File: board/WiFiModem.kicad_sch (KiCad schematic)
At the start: 49 parts, among them J1 DB9_Female, J2 DB25_Female, J3 Barrel_Jack_Switch, J4 PRG, SW1 SW_Push, SW2 SW_Push, U1 ESP-12E, U2 LM7805_TO220, U3 MAX232, U4 LT1117-3.3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

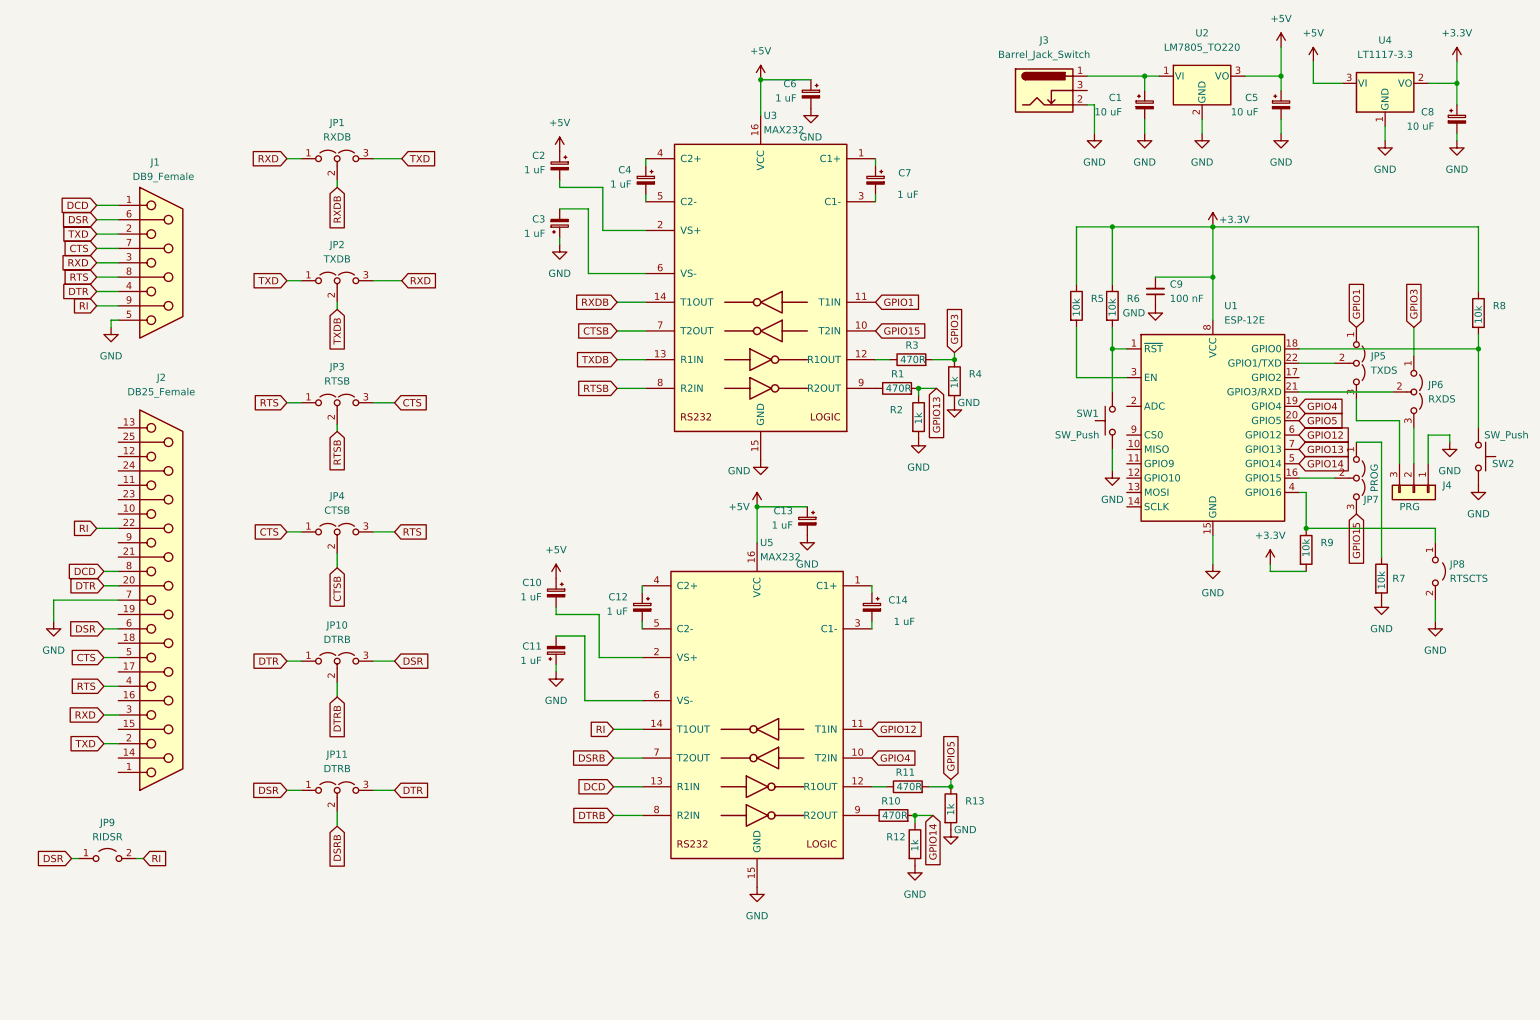
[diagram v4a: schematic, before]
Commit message: Fixed GPIO15 booting issue, changed DCD/DSR/DTR jumper
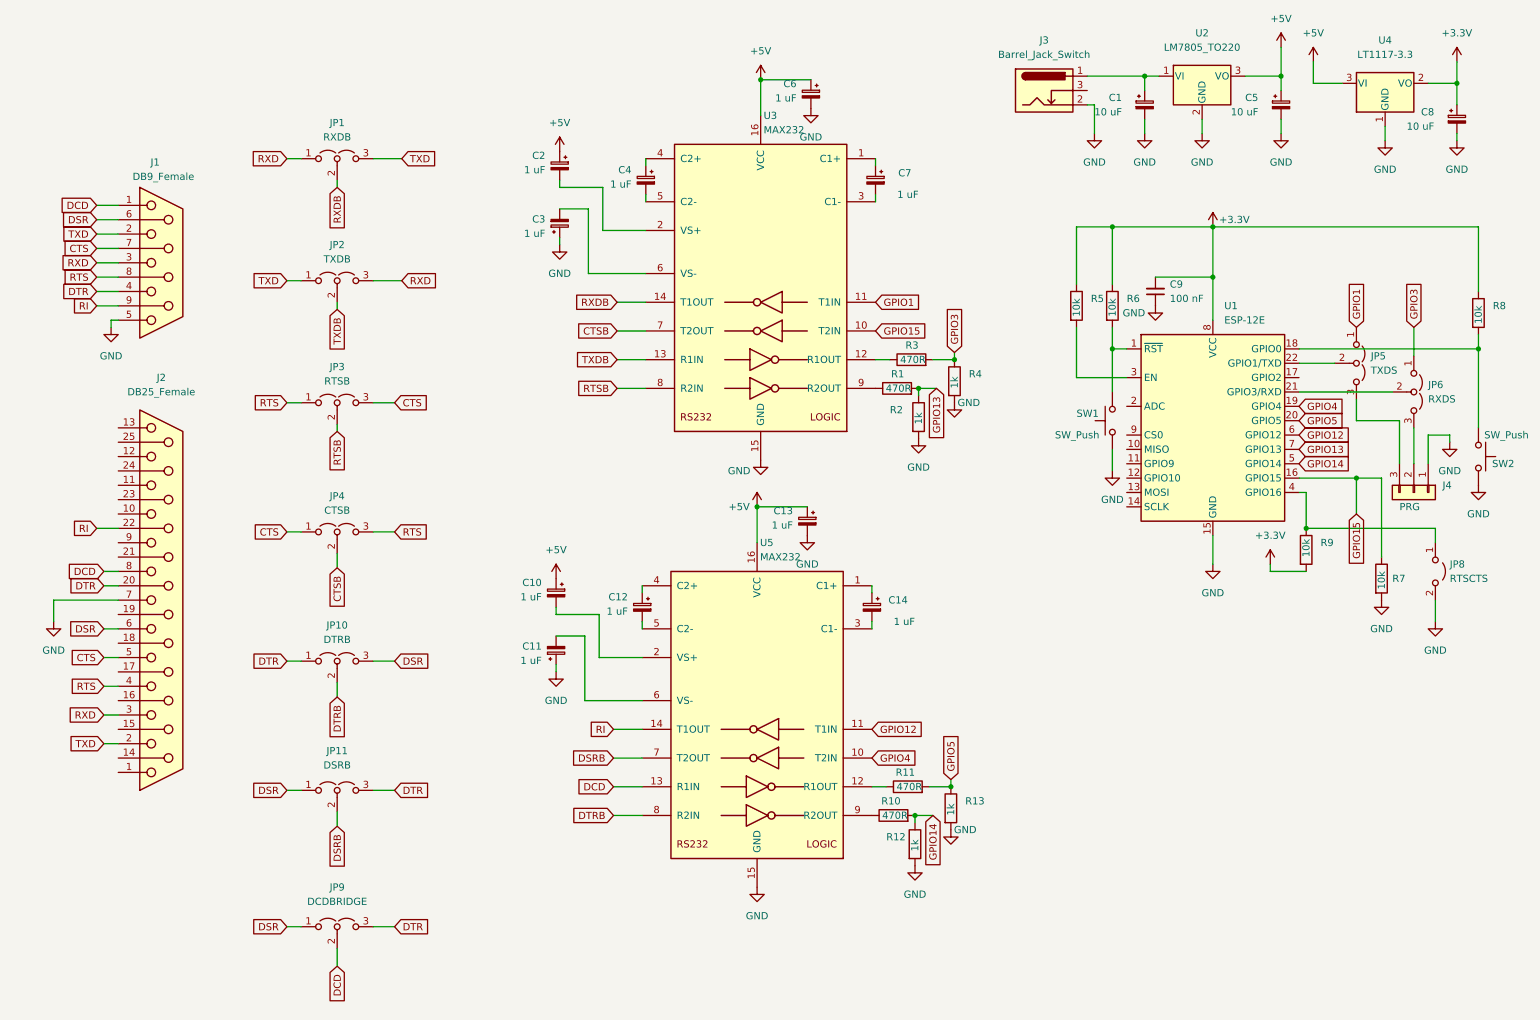
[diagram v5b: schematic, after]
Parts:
- removed JP7: PROG, Connector_PinHeader_2.54mm:PinHeader_1x03_P2.54mm_Vertical, symbol Jumper:Jumper_3_Open
- removed JP9: RIDSR, Connector_PinHeader_2.54mm:PinHeader_1x02_P2.54mm_Vertical, symbol Jumper:Jumper_2_Open
- added JP9: DCDBRIDGE, Connector_PinHeader_2.54mm:PinHeader_1x03_P2.54mm_Vertical, symbol Jumper:Jumper_3_Open
- JP11: value DTRB -> DSRB
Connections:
- net DCD: now also JP9.2 (C)
- net DSR: now also JP9.1 (A)
- net DTR: now also JP9.3 (B)
- net GPIO15: now also R7.1, U1.16 (GPIO15)
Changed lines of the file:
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@@
   (junction (at 175.895 156.21) (diameter 0) (color 0 0 0 0)
   )
+  (junction (at 254 96.52) (diameter 0) (color 0 0 0 0)
+  )
   (wire (pts (xy 80.01 151.765) (xy 83.82 151.765))
     (stroke (width 0) (type default) (color 0 0 0 0))
@@
     (stroke (width 0) (type default) (color 0 0 0 0))
   )
-  (wire (pts (xy 26.67 163.83) (xy 27.94 163.83))
-    (stroke (width 0) (type default) (color 0 0 0 0))
-  )
   (wire (pts (xy 176.53 80.645) (xy 179.705 80.645))
     (stroke (width 0) (type default) (color 0 0 0 0))
@@
     (stroke (width 0) (type default) (color 0 0 0 0))
   )
+  (wire (pts (xy 254 96.52) (xy 254 102.87))
+    (stroke (width 0) (type default) (color 0 0 0 0))
+  )
   (wire (pts (xy 147.955 107.95) (xy 147.955 101.6))
     (stroke (width 0) (type default) (color 0 0 0 0))
@@
     (stroke (width 0) (type default) (color 0 0 0 0))
   )
+  (wire (pts (xy 80.01 175.895) (xy 83.82 175.895))
+    (stroke (width 0) (type default) (color 0 0 0 0))
+  )
   (wire (pts (xy 112.395 129.54) (xy 112.395 130.81))
     (stroke (width 0) (type default) (color 0 0 0 0))
@@
     (stroke (width 0) (type default) (color 0 0 0 0))
   )
+  (wire (pts (xy 64.77 175.895) (xy 67.31 175.895))
+    (stroke (width 0) (type default) (color 0 0 0 0))
+  )
   (wire (pts (xy 245.11 105.41) (xy 267.97 105.41))
     (stroke (width 0) (type default) (color 0 0 0 0))
@@
     (stroke (width 0) (type default) (color 0 0 0 0))
   )
-  (wire (pts (xy 258.445 110.49) (xy 258.445 90.17))
+  (wire (pts (xy 254 96.52) (xy 258.445 96.52))
+    (stroke (width 0) (type default) (color 0 0 0 0))
+  )
+  (wire (pts (xy 258.445 110.49) (xy 258.445 96.52))
     (stroke (width 0) (type default) (color 0 0 0 0))
   )
@@
     (stroke (width 0) (type default) (color 0 0 0 0))
   )
-  (wire (pts (xy 38.1 163.83) (xy 39.37 163.83))
-    (stroke (width 0) (type default) (color 0 0 0 0))
-  )
   (wire (pts (xy 245.11 99.06) (xy 245.11 105.41))
     (stroke (width 0) (type default) (color 0 0 0 0))
@@
     (stroke (width 0) (type default) (color 0 0 0 0))
   )
-  (wire (pts (xy 243.84 96.52) (xy 250.19 96.52))
+  (wire (pts (xy 243.84 96.52) (xy 254 96.52))
     (stroke (width 0) (type default) (color 0 0 0 0))
   )
@@
     (stroke (width 0) (type default) (color 0 0 0 0))
   )
+  (wire (pts (xy 73.66 179.705) (xy 73.66 182.88))
+    (stroke (width 0) (type default) (color 0 0 0 0))
+  )
   (wire (pts (xy 168.91 41.275) (xy 168.91 40.005))
     (stroke (width 0) (type default) (color 0 0 0 0))
@@
   )
   (wire (pts (xy 122.555 156.21) (xy 127.635 156.21))
-    (stroke (width 0) (type default) (color 0 0 0 0))
-  )
-  (wire (pts (xy 254 90.17) (xy 258.445 90.17))
     (stroke (width 0) (type default) (color 0 0 0 0))
   )
@@
     )
   )
-  (global_label "DSR" (shape input) (at 26.67 163.83 180) (fields_autoplaced)
-    (effects (font (size 1.27 1.27)) (justify right))
-    (property "Intersheet References" "${INTERSHEET_REFS}" (id 0) (at 20.5074 163.9094 0)
+  (global_label "DSR" (shape input) (at 64.77 175.895 180) (fields_autoplaced)
+    (effects (font (size 1.27 1.27)) (justify right))
+    (property "Intersheet References" "${INTERSHEET_REFS}" (id 0) (at 58.6074 175.9744 0)
       (effects (font (size 1.27 1.27)) (justify right) hide)
     )
@@
     )
   )
-  (global_label "RI" (shape input) (at 39.37 163.83 0) (fields_autoplaced)
-    (effects (font (size 1.27 1.27)) (justify left))
-    (property "Intersheet References" "${INTERSHEET_REFS}" (id 0) (at 43.6579 163.9094 0)
-      (effects (font (size 1.27 1.27)) (justify left) hide)
+  (global_label "DCD" (shape input) (at 73.66 182.88 270) (fields_autoplaced)
+    (effects (font (size 1.27 1.27)) (justify right))
+    (property "Intersheet References" "${INTERSHEET_REFS}" (id 0) (at 73.5806 189.1031 90)
+      (effects (font (size 1.27 1.27)) (justify right) hide)
     )
   )
@@
     (property "Intersheet References" "${INTERSHEET_REFS}" (id 0) (at 73.5806 73.8052 90)
       (effects (font (size 1.27 1.27)) (justify right) hide)
+    )
+  )
+  (global_label "DTR" (shape input) (at 83.82 175.895 0) (fields_autoplaced)
+    (effects (font (size 1.27 1.27)) (justify left))
+    (property "Intersheet References" "${INTERSHEET_REFS}" (id 0) (at 89.7407 175.8156 0)
+      (effects (font (size 1.27 1.27)) (justify left) hide)
     )
   )
@@
   (symbol (lib_id "Jumper:Jumper_3_Open") (at 73.66 151.765 0) (unit 1)
     (in_bom yes) (on_board yes) (fields_autoplaced)
-    (property "Reference" "JP11" (id 0) (at 73.66 145.415 0))
-    (property "Value" "DTRB" (id 1) (at 73.66 147.955 0))
+    (property "Reference" "JP11" (id 0) (at 73.66 144.78 0))
+    (property "Value" "DSRB" (id 1) (at 73.66 147.32 0))
     (property "Footprint" "Connector_PinHeader_2.54mm:PinHeader_1x03_P2.54mm_Vertical" (id 2) (at 73.66 151.765 0)
       (effects (font (size 1.27 1.27)) hide)
@@
     )
     (pin "1")
-  )
-  (symbol (lib_id "Jumper:Jumper_2_Open") (at 33.02 163.83 0) (unit 1)
-    (in_bom yes) (on_board yes) (fields_autoplaced)
-    (property "Reference" "JP9" (id 0) (at 33.02 157.48 0))
-    (property "Value" "RIDSR" (id 1) (at 33.02 160.02 0))
-    (property "Footprint" "Connector_PinHeader_2.54mm:PinHeader_1x02_P2.54mm_Vertical" (id 2) (at 33.02 163.83 0)
-      (effects (font (size 1.27 1.27)) hide)
-    )
-    (property "Datasheet" "~" (id 3) (at 33.02 163.83 0)
-      (effects (font (size 1.27 1.27)) hide)
-    )
-    (pin "1")
-    (pin "2")
   )
   (symbol (lib_id "power:GND") (at 240.665 35.56 0) (mirror y) (unit 1)
@@
     (pin "1")
   )
+  (symbol (lib_id "Jumper:Jumper_3_Open") (at 73.66 175.895 0) (unit 1)
+    (in_bom yes) (on_board yes) (fields_autoplaced)
+    (property "Reference" "JP9" (id 0) (at 73.66 168.91 0))
+    (property "Value" "DCDBRIDGE" (id 1) (at 73.66 171.45 0))
+    (property "Footprint" "Connector_PinHeader_2.54mm:PinHeader_1x03_P2.54mm_Vertical" (id 2) (at 73.66 175.895 0)
+      (effects (font (size 1.27 1.27)) hide)
+    )
+    (property "Datasheet" "~" (id 3) (at 73.66 175.895 0)
+      (effects (font (size 1.27 1.27)) hide)
+    )
+    (pin "1")
+    (pin "2")
+    (pin "3")
+  )
   (symbol (lib_id "power:+5V") (at 240.665 20.32 0) (mirror y) (unit 1)
     (in_bom yes) (on_board yes) (fields_autoplaced)
@@
     )
     (pin "1")
-  )
-  (symbol (lib_id "Jumper:Jumper_3_Open") (at 254 96.52 270) (unit 1)
-    (in_bom yes) (on_board yes)
-    (property "Reference" "JP7" (id 0) (at 255.27 100.33 90)
-      (effects (font (size 1.27 1.27)) (justify left))
-    )
-    (property "Value" "PROG" (id 1) (at 257.175 93.98 0)
-      (effects (font (size 1.27 1.27)) (justify left))
-    )
-    (property "Footprint" "Connector_PinHeader_2.54mm:PinHeader_1x03_P2.54mm_Vertical" (id 2) (at 254 96.52 0)
-      (effects (font (size 1.27 1.27)) hide)
-    )
-    (property "Datasheet" "~" (id 3) (at 254 96.52 0)
-      (effects (font (size 1.27 1.27)) hide)
-    )
-    (pin "1")
-    (pin "2")
-    (pin "3")
   )
   (symbol (lib_id "power:GND") (at 259.08 36.83 0) (mirror y) (unit 1)
@@
       (reference "JP6") (unit 1) (value "RXDS") (footprint "Connector_PinHeader_2.54mm:PinHeader_1x03_P2.54mm_Vertical")
     )
-    (path "/e384ffec-bb2c-46ec-b097-3f0cea4d11a2"
-      (reference "JP7") (unit 1) (value "PROG") (footprint "Connector_PinHeader_2.54mm:PinHeader_1x03_P2.54mm_Vertical")
-    )
     (path "/2cfe946b-ef42-4712-aba1-8371f5f81b04"
       (reference "JP8") (unit 1) (value "RTSCTS") (footprint "Connector_PinHeader_2.54mm:PinHeader_1x02_P2.54mm_Vertical")
     )
-    (path "/6e6f41cf-eea7-4319-a566-0c19ed9572c2"
-      (reference "JP9") (unit 1) (value "RIDSR") (footprint "Connector_PinHeader_2.54mm:PinHeader_1x02_P2.54mm_Vertical")
+    (path "/dafbc4d4-726b-47c7-b074-8d381c5f7477"
+      (reference "JP9") (unit 1) (value "DCDBRIDGE") (footprint "Connector_PinHeader_2.54mm:PinHeader_1x03_P2.54mm_Vertical")
     )
     (path "/d066ecb3-5158-4d54-9143-8be97669845b"
@@
     )
     (path "/5247d984-7f9f-417f-8e7e-3a014e2c2aca"
-      (reference "JP11") (unit 1) (value "DTRB") (footprint "Connector_PinHeader_2.54mm:PinHeader_1x03_P2.54mm_Vertical")
+      (reference "JP11") (unit 1) (value "DSRB") (footprint "Connector_PinHeader_2.54mm:PinHeader_1x03_P2.54mm_Vertical")
     )
     (path "/ed4f2a97-7862-4c00-9260-110c4aa8ea06"

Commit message: Fixed DCD and DB25 pinouts
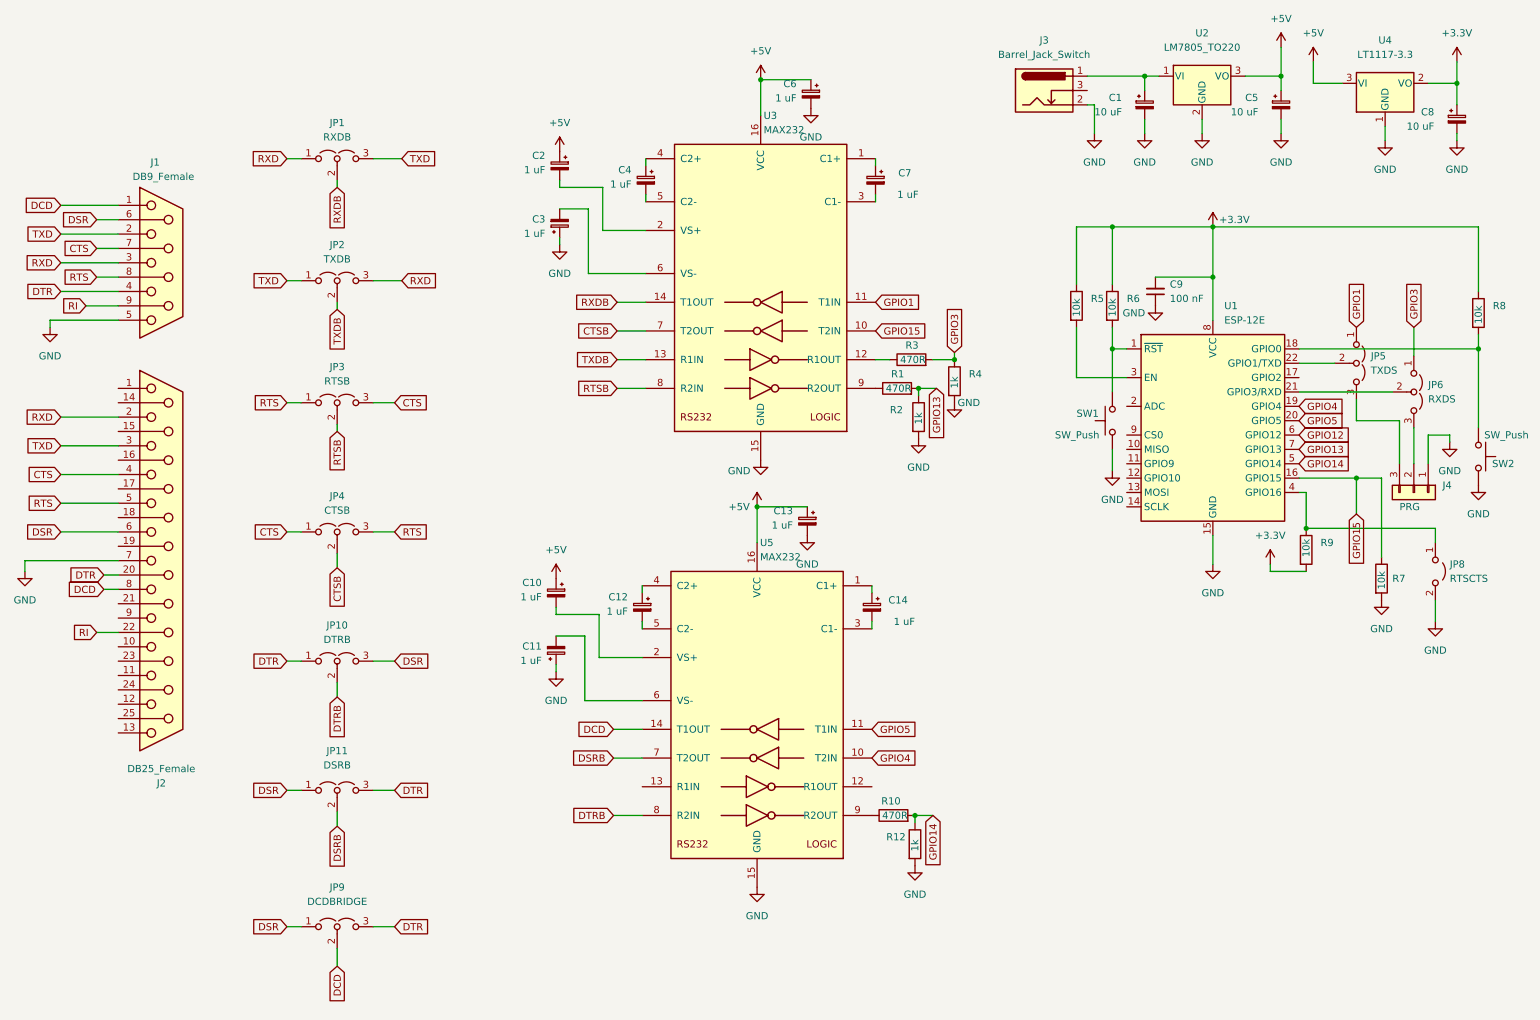
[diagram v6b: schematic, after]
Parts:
- removed R11: 470R, Resistor_THT:R_Axial_DIN0207_L6.3mm_D2.5mm_P7.62mm_Horizontal, symbol Device:R
- removed R13: 1k, Resistor_THT:R_Axial_DIN0207_L6.3mm_D2.5mm_P7.62mm_Horizontal, symbol Device:R
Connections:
- net CTS: now also J2.4; no longer J2.5
- net DCD: now also U5.14 (T1OUT); no longer U5.13 (R1IN)
- net GPIO12: no longer U5.11 (T1IN)
- net GPIO5: now also U5.11 (T1IN)
- net RI: no longer U5.14 (T1OUT)
- net RTS: now also J2.5; no longer J2.4
- net RXD: now also J2.2; no longer J2.3
- net TXD: now also J2.3; no longer J2.2
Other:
- moved on the sheet: J2
